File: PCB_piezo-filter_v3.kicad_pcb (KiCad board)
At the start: 2 copper layers, 48 parts, among them J1 Conn_01x02_Pin, J2 Conn_01x03_Pin, J3 Conn_01x01_Pin, J4 Conn_01x01_Pin, J5 Conn_01x01_Pin, J6 Conn_01x01_Pin, U1 TL062, U2 TLC2262CP, U3 TLC2262CP

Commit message: pcb connection
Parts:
- moved C21 154.4 mm to (207.6, 96.1), turned to -90 degrees
- moved R4 142.7 mm to (196.2, 126.8), turned to 180 degrees
- moved C8 141.0 mm to (212.0, 124.4), turned to 90 degrees
- moved C18 138.6 mm to (216.5, 120.9), turned to -90 degrees
- moved C17 138.2 mm to (218.1, 109.0), turned to 90 degrees
- moved C16 134.5 mm to (213.3, 109.0), turned to 90 degrees
- moved J6 133.9 mm to (223.6, 124.1)
- moved R15 132.8 mm to (218.8, 112.6), turned to 180 degrees
- moved R14 128.0 mm to (211.1, 117.4)
- moved R5 127.0 mm to (185.5, 126.8)
- moved R12 125.7 mm to (211.0, 102.0)
- moved C9 124.0 mm to (199.7, 113.7)
- moved R13 123.0 mm to (207.8, 107.1), turned to -90 degrees
- moved R11 120.5 mm to (204.4, 101.7), turned to -90 degrees
- moved R10 117.5 mm to (199.6, 101.8), turned to -90 degrees
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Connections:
- net U2_1IN+ renamed Net-(U2A-+)
- C1 pad 1: Net-(J2-Pin_1) -> Net-(J2-Pin_2)
- C19 pad 2: Net-(J2-Pin_1) -> Net-(J2-Pin_2)
- C20 pad 2: Net-(J2-Pin_2) -> Net-(J2-Pin_3)
- J2 pad 1: Net-(J2-Pin_1) -> VEE
- J2 pad 3: VEE -> Net-(J2-Pin_3)
- R1 pad 2: Net-(J2-Pin_1) -> Net-(J2-Pin_2)
- R2 pad 2: Net-(J2-Pin_2) -> Net-(J2-Pin_3)
- R3 pad 2: Net-(J2-Pin_1) -> Net-(J2-Pin_2)
- U1 pad 2: Net-(J2-Pin_2) -> Net-(J2-Pin_3)
- U1 pad 3: Net-(J2-Pin_1) -> Net-(J2-Pin_2)
- U1 pad 6: Net-(J2-Pin_1) -> Net-(J2-Pin_2)
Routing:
- net VCC: track 6.20 -> 186.4 mm, vias 0 -> 1
- net VGND: track 0.00 -> 148.0 mm
- net U2_1OUT: track 0.00 -> 79.5 mm, vias 0 -> 2
- net U2_2OUT: track 0.00 -> 66.2 mm
- net Net-(C12-Pad2): track 0.00 -> 57.8 mm
- net Net-(J3-Pin_1): track 6.14 -> 62.1 mm, vias 0 -> 1
- net Net-(U2B-+): track 0.00 -> 47.8 mm
- net Net-(C10-Pad2): track 0.00 -> 42.5 mm
- net Net-(J2-Pin_1): track 32.7 -> 0.00 mm
- net Net-(U2A-+): track 0.00 -> 28.8 mm
- net Net-(C16-Pad1): track 0.00 -> 26.3 mm
- net Net-(C16-Pad2): track 0.00 -> 23.8 mm
- net Net-(J2-Pin_2): track 13.3 -> 35.6 mm
- net Net-(U3A--): track 0.00 -> 19.0 mm
- net Net-(J2-Pin_3): track 0.00 -> 17.9 mm
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- added copper zone on B.Cu, net VEE
- added copper zone on F.Cu, net VEE
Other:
- board outline added: 115.5 x 39.5 mm

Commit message: last details
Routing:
- net Net-(J6-Pin_1): track 13.5 -> 15.5 mm, vias 0 -> 1
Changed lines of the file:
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@@
 			(drillshape 0)
 			(scaleselection 1)
-			(outputdirectory "")
+			(outputdirectory "/home/david/Documents/LTspice/PCB_filter/PCB_piezo-filter_v4/")
 		)
 	)
@@
 	)
 	(segment
-		(start 218.74 119.29)
-		(end 223.54 124.09)
+		(start 218.74 117.39)
+		(end 218.74 122.66)
 		(width 1)
 		(layer "F.Cu")
@@
 	)
 	(segment
-		(start 223.54 124.09)
-		(end 223.58 124.09)
+		(start 218.74 122.66)
+		(end 220.02 123.94)
 		(width 1)
 		(layer "F.Cu")
 		(net 14)
 	)
-	(segment
-		(start 218.74 117.39)
-		(end 218.74 119.29)
-		(width 1)
-		(layer "F.Cu")
+	(via
+		(at 220.02 123.94)
+		(size 1.8)
+		(drill 0.4)
+		(layers "F.Cu" "B.Cu")
 		(net 14)
 	)
@@
 		(width 1)
 		(layer "B.Cu")
+		(net 14)
+	)
+	(segment
+		(start 220.02 123.94)
+		(end 223.43 123.94)
+		(width 1)
+		(layer "B.Cu")
+		(net 14)
+	)
+	(segment
+		(start 223.43 123.94)
+		(end 223.58 124.09)
+		(width 1)
+		(layer "B.Cu")

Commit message: update clearance to 1.6
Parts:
- moved J1 2.10 mm to (223.8, 119.1)
- moved J6 2.10 mm to (223.9, 126.2)
- moved C21 1.79 mm to (209.1, 95.2)
- moved R4 0.99 mm to (196.4, 127.8)
- moved R5 0.99 mm to (185.7, 127.8)
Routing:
- net VEE: track 0.00 -> 18.9 mm, vias 0 -> 1
- net Net-(J6-Pin_1): track 15.5 -> 18.0 mm
- net VCC: track 186.4 -> 187.8 mm
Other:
- board size 115.5 x 39.5 mm -> 118.2 x 41.4 mm

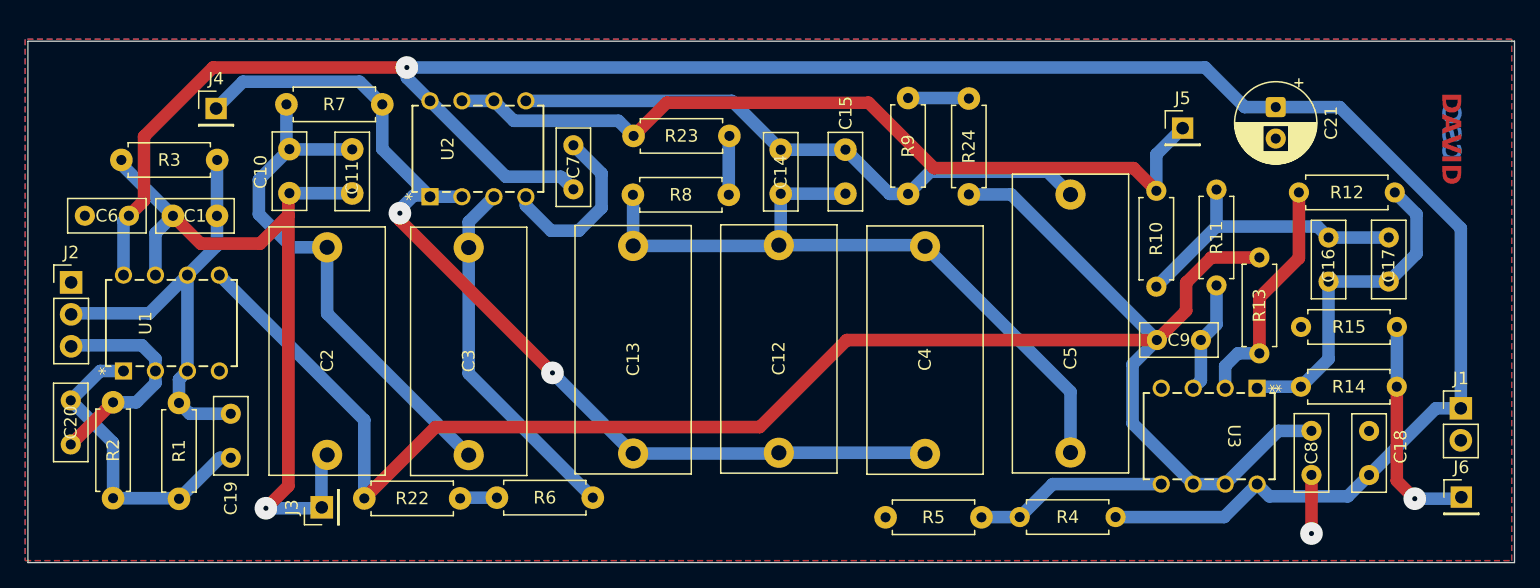
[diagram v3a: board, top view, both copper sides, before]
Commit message: updated clearance path holes to 1.8 and 0.8
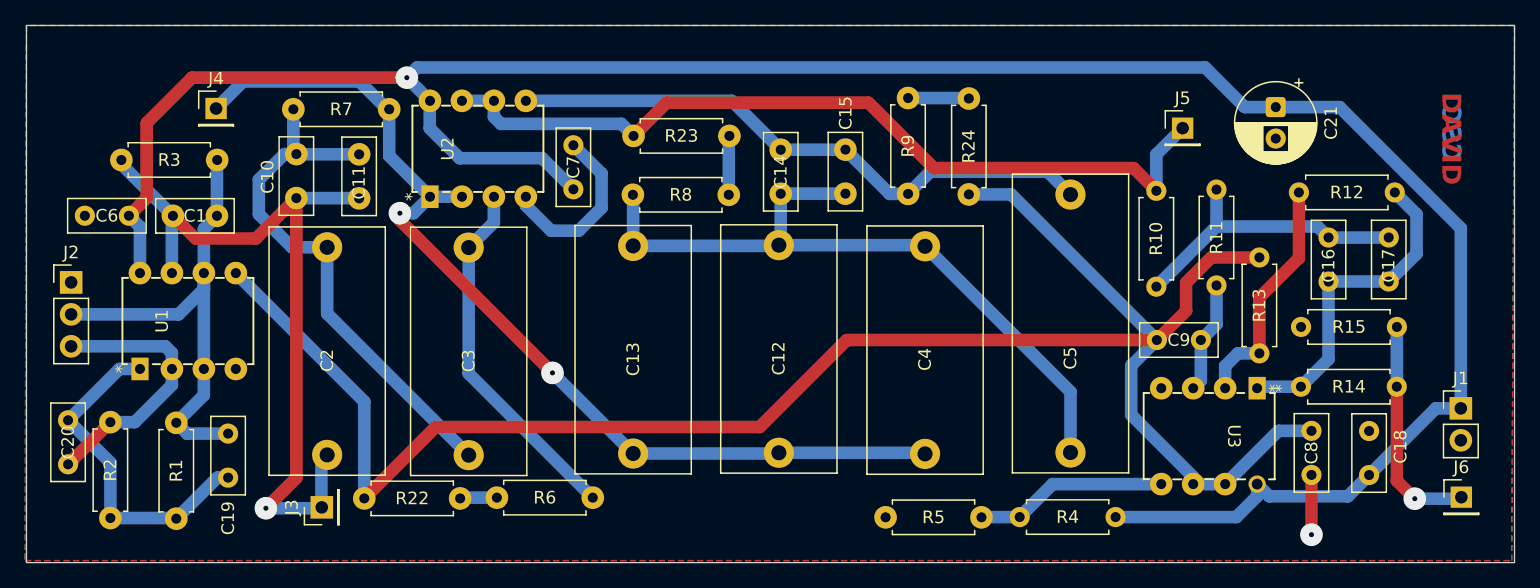
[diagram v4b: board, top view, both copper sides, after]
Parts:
- moved R1 1.59 mm to (121.7, 127.9)
- moved C19 1.59 mm to (125.9, 124.6)
- moved C20 1.59 mm to (113.1, 120.1)
- moved R2 1.59 mm to (116.5, 127.8)
- moved U1 1.32 mm to (118.8, 116.0)
- moved C10 0.67 mm to (131.3, 102.4)
- moved C11 0.67 mm to (136.3, 102.4)
- moved R7 0.67 mm to (138.7, 95.3)
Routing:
- net Net-(J2-Pin_2): track 35.6 -> 39.4 mm
- net Net-(J2-Pin_3): track 17.9 -> 21.6 mm
- net Net-(C19-Pad1): track 25.1 -> 27.3 mm
- net VCC: track 187.8 -> 189.4 mm
- net U2_2OUT: track 66.2 -> 66.9 mm
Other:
- board size 118.2 x 41.4 mm -> 118.3 x 42.7 mm
